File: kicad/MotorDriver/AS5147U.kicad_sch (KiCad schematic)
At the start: 1 part, among them U7 AS5147U

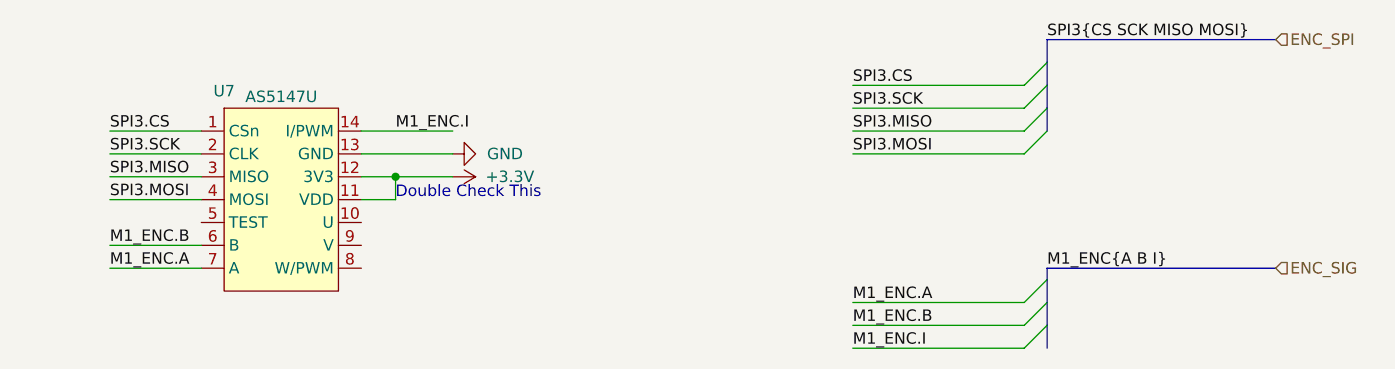
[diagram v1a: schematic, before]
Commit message: Updated the planetary gearbox design. It is much better with retaining rings and bearing support. 95% done with the PCB routing. Need to just do a final routing check and i think I can put the order in
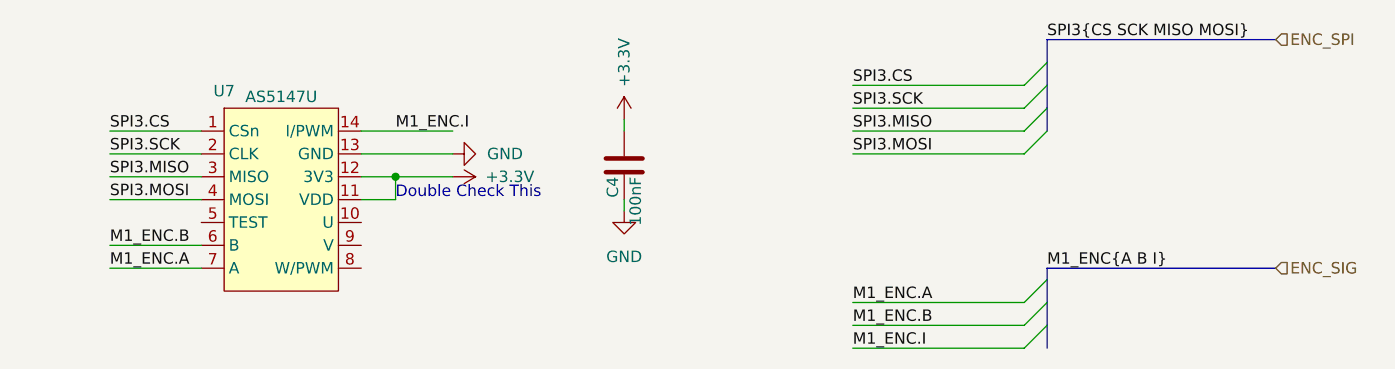
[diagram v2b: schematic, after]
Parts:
- added C4: 100nF, Capacitor_SMD:C_0603_1608Metric, symbol Device:C
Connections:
- net +3.3V: now also C4.2
- net GND: now also C4.1
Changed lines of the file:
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@@
+    (stroke (width 0) (type default))
+  )
+  (wire (pts (xy 177.8 72.39) (xy 177.8 73.66))
     (stroke (width 0) (type default))
   )
@@
   )
   (wire (pts (xy 203.2 71.12) (xy 222.25 71.12))
+    (stroke (width 0) (type default))
+  )
+  (wire (pts (xy 177.8 82.55) (xy 177.8 81.28))
     (stroke (width 0) (type default))
   )
@@
     (effects (font (size 1.27 1.27)) (justify left bottom))
   )
-  (label "M1_ENC.A" (at 203.2 92.71 0)
+  (label "M1_ENC.A" (at 203.2 92.71 0) (fields_autoplaced)
     (effects (font (size 1.27 1.27)) (justify left bottom))
   )
@@
     (effects (font (size 1.27 1.27)) (justify left bottom))
   )
-  (label "SPI3.SCK" (at 203.2 71.12 0)
+  (label "SPI3.SCK" (at 203.2 71.12 0) (fields_autoplaced)
     (effects (font (size 1.27 1.27)) (justify left bottom))
   )
@@
     (effects (font (size 1.27 1.27)) (justify left bottom))
   )
-  (label "SPI3.MISO" (at 203.2 73.66 0)
+  (label "SPI3.MISO" (at 203.2 73.66 0) (fields_autoplaced)
     (effects (font (size 1.27 1.27)) (justify left bottom))
   )
@@
     (effects (font (size 1.27 1.27)) (justify left bottom))
   )
-  (label "SPI3.CS" (at 203.2 68.58 0)
+  (label "SPI3.CS" (at 203.2 68.58 0) (fields_autoplaced)
     (effects (font (size 1.27 1.27)) (justify left bottom))
   )
@@
     (effects (font (size 1.27 1.27)) (justify left))
   )
+  (symbol (lib_id "Device:C") (at 177.8 77.47 180) (unit 1)
+    (in_bom yes) (on_board yes) (dnp no)
+    (property "Reference" "C4" (at 176.53 78.74 90)
+      (effects (font (size 1.27 1.27)) (justify left))
+    )
+    (property "Value" "100nF" (at 179.07 78.74 90)
+      (effects (font (size 1.27 1.27)) (justify left))
+    )
+    (property "Footprint" "Capacitor_SMD:C_0603_1608Metric" (at 176.8348 73.66 0)
+      (effects (font (size 1.27 1.27)) hide)
+    )
+    (property "Datasheet" "~" (at 177.8 77.47 0)
+      (effects (font (size 1.27 1.27)) hide)
+    )
+    (pin "2")
+    (pin "1")
+    (instances
+      (project "MotorDriver"
+        (path "/1fa4c72f-b85f-4d78-9713-26aa572ca2e5"
+          (reference "C4") (unit 1)
+        )
+        (path "/1fa4c72f-b85f-4d78-9713-26aa572ca2e5/c363089b-1b0b-4509-af19-a6f84e71682e"
+          (reference "C28") (unit 1)
+        )
+        (path "/1fa4c72f-b85f-4d78-9713-26aa572ca2e5/a6e3eacb-7b2e-4ad7-94d2-e19606b91cfd"
+          (reference "C3") (unit 1)
+        )
+        (path "/1fa4c72f-b85f-4d78-9713-26aa572ca2e5/bb03fcb5-c814-4162-9fb3-5a1cbb252e46"
+          (reference "C10") (unit 1)
+        )
+      )
+    )
+  )
+  (symbol (lib_id "power:GND") (at 177.8 82.55 0) (unit 1)
+    (in_bom yes) (on_board yes) (dnp no) (fields_autoplaced)
+    (property "Reference" "#PWR037" (at 177.8 88.9 0)
+      (effects (font (size 1.27 1.27)) hide)
+    )
+    (property "Value" "GND" (at 177.8 87.63 0)
+      (effects (font (size 1.27 1.27)))
+    )
+    (property "Footprint" "" (at 177.8 82.55 0)
+      (effects (font (size 1.27 1.27)) hide)
+    )
+    (property "Datasheet" "" (at 177.8 82.55 0)
+      (effects (font (size 1.27 1.27)) hide)
+    )
+    (pin "1")
+    (instances
+      (project "MotorDriver"
+        (path "/1fa4c72f-b85f-4d78-9713-26aa572ca2e5"
+          (reference "#PWR037") (unit 1)
+        )
+        (path "/1fa4c72f-b85f-4d78-9713-26aa572ca2e5/bb03fcb5-c814-4162-9fb3-5a1cbb252e46"
+          (reference "#PWR015") (unit 1)
+        )
+      )
+    )
+  )
+  (symbol (lib_id "power:+3.3V") (at 177.8 72.39 0) (unit 1)
+    (in_bom yes) (on_board yes) (dnp no)
+    (property "Reference" "#PWR036" (at 177.8 76.2 0)
+      (effects (font (size 1.27 1.27)) hide)
+    )
+    (property "Value" "+3.3V" (at 177.8 66.04 90)
+      (effects (font (size 1.27 1.27)))
+    )
+    (property "Footprint" "" (at 177.8 72.39 0)
+      (effects (font (size 1.27 1.27)) hide)
+    )
+    (property "Datasheet" "" (at 177.8 72.39 0)
+      (effects (font (size 1.27 1.27)) hide)
+    )
+    (pin "1")
+    (instances
+      (project "MotorDriver"
+        (path "/1fa4c72f-b85f-4d78-9713-26aa572ca2e5"
+          (reference "#PWR036") (unit 1)
+        )
+        (path "/1fa4c72f-b85f-4d78-9713-26aa572ca2e5/bb03fcb5-c814-4162-9fb3-5a1cbb252e46"
+          (reference "#PWR012") (unit 1)
+        )
+      )
+    )
+  )
   (symbol (lib_id "TylerLib:AS5147U-HTSM") (at 139.7 69.85 0) (unit 1)

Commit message: PCB ordered
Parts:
- C4: value 100nF -> 0.1uF
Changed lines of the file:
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@@
   (symbol (lib_id "Device:C") (at 177.8 77.47 180) (unit 1)
     (in_bom yes) (on_board yes) (dnp no)
-    (property "Reference" "C4" (at 176.53 78.74 90)
+    (property "Reference" "C4" (at 182.245 74.93 0)
       (effects (font (size 1.27 1.27)) (justify left))
     )
-    (property "Value" "100nF" (at 179.07 78.74 90)
+    (property "Value" "0.1uF" (at 184.785 80.01 0)
       (effects (font (size 1.27 1.27)) (justify left))
     )
@@
       (effects (font (size 1.27 1.27)) hide)
     )
-    (property "Datasheet" "~" (at 177.8 77.47 0)
+    (property "Datasheet" "https://www.digikey.com/en/products/detail/samsung-electro-mechanics/CL10B104KB8NNWC/3887593" (at 177.8 77.47 0)
       (effects (font (size 1.27 1.27)) hide)
     )
@@
       (effects (font (size 1.27 1.27)) hide)
     )
-    (property "Datasheet" "" (at 139.7 69.85 0)
+    (property "Datasheet" "https://www.digikey.com/en/products/detail/ams-osram-usa-inc/AS5147U-HTSM/10324300" (at 139.7 69.85 0)
       (effects (font (size 1.27 1.27)) hide)
     )

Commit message: Working on some of the solidworks model, new urdf, working on the motor drive board a little
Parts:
- added TP2 (x7): TestPoint, TestPoint:TestPoint_Pad_D1.0mm, symbol Connector:TestPoint
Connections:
- net M1_ENC.A: now also TP2.1
- net M1_ENC.B: now also TP2.1
- net M1_ENC.I: now also TP2.1
- net SPI3.CS: now also TP2.1
- net SPI3.MISO: now also TP2.1
- net SPI3.MOSI: now also TP2.1
- net SPI3.SCK: now also TP2.1
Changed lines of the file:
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@@
     (stroke (width 0) (type default))
   )
-  (wire (pts (xy 130.81 78.74) (xy 120.65 78.74))
+  (wire (pts (xy 130.81 78.74) (xy 116.84 78.74))
     (stroke (width 0) (type default))
   )
@@
     (stroke (width 0) (type default))
   )
-  (wire (pts (xy 130.81 76.2) (xy 120.65 76.2))
+  (wire (pts (xy 130.81 76.2) (xy 118.745 76.2))
     (stroke (width 0) (type default))
   )
@@
     (stroke (width 0) (type default))
   )
-  (wire (pts (xy 130.81 88.9) (xy 120.65 88.9))
+  (wire (pts (xy 130.81 88.9) (xy 118.745 88.9))
     (stroke (width 0) (type default))
   )
@@
   (hierarchical_label "ENC_SIG" (shape input) (at 250.19 88.9 0) (fields_autoplaced)
     (effects (font (size 1.27 1.27)) (justify left))
+  )
+  (symbol (lib_id "Connector:TestPoint") (at 120.65 73.66 90) (unit 1)
+    (in_bom yes) (on_board yes) (dnp no)
+    (property "Reference" "TP2" (at 115.57 74.93 0)
+      (effects (font (size 1.27 1.27)) (justify left))
+    )
+    (property "Value" "TestPoint" (at 118.618 71.12 0)
+      (effects (font (size 1.27 1.27)) (justify left) hide)
+    )
+    (property "Footprint" "TestPoint:TestPoint_Pad_D1.0mm" (at 120.65 68.58 0)
+      (effects (font (size 1.27 1.27)) hide)
+    )
+    (property "Datasheet" "~" (at 120.65 68.58 0)
+      (effects (font (size 1.27 1.27)) hide)
+    )
+    (pin "1")
+    (instances
+      (project "MotorDriver"
+        (path "/1fa4c72f-b85f-4d78-9713-26aa572ca2e5"
+          (reference "TP2") (unit 1)
+        )
+        (path "/1fa4c72f-b85f-4d78-9713-26aa572ca2e5/c363089b-1b0b-4509-af19-a6f84e71682e"
+          (reference "TP5") (unit 1)
+        )
+        (path "/1fa4c72f-b85f-4d78-9713-26aa572ca2e5/bb03fcb5-c814-4162-9fb3-5a1cbb252e46"
+          (reference "TP1") (unit 1)
+        )
+      )
+    )
   )
   (symbol (lib_id "Device:C") (at 177.8 77.47 180) (unit 1)
@@
         (path "/1fa4c72f-b85f-4d78-9713-26aa572ca2e5/bb03fcb5-c814-4162-9fb3-5a1cbb252e46"
           (reference "#PWR012") (unit 1)
+        )
+      )
+    )
+  )
+  (symbol (lib_id "Connector:TestPoint") (at 116.84 78.74 90) (unit 1)
+    (in_bom yes) (on_board yes) (dnp no)
+    (property "Reference" "TP2" (at 111.76 80.01 0)
+      (effects (font (size 1.27 1.27)) (justify left))
+    )
+    (property "Value" "TestPoint" (at 114.808 76.2 0)
+      (effects (font (size 1.27 1.27)) (justify left) hide)
+    )
+    (property "Footprint" "TestPoint:TestPoint_Pad_D1.0mm" (at 116.84 73.66 0)
+      (effects (font (size 1.27 1.27)) hide)
+    )
+    (property "Datasheet" "~" (at 116.84 73.66 0)
+      (effects (font (size 1.27 1.27)) hide)
+    )
+    (pin "1")
+    (instances
+      (project "MotorDriver"
+        (path "/1fa4c72f-b85f-4d78-9713-26aa572ca2e5"
+          (reference "TP2") (unit 1)
+        )
+        (path "/1fa4c72f-b85f-4d78-9713-26aa572ca2e5/c363089b-1b0b-4509-af19-a6f84e71682e"
+          (reference "TP5") (unit 1)
+        )
+        (path "/1fa4c72f-b85f-4d78-9713-26aa572ca2e5/bb03fcb5-c814-4162-9fb3-5a1cbb252e46"
+          (reference "TP3") (unit 1)
         )
       )
@@
     )
   )
+  (symbol (lib_id "Connector:TestPoint") (at 120.65 86.36 90) (unit 1)
+    (in_bom yes) (on_board yes) (dnp no)
+    (property "Reference" "TP2" (at 115.57 87.63 0)
+      (effects (font (size 1.27 1.27)) (justify left))
+    )
+    (property "Value" "TestPoint" (at 118.618 83.82 0)
+      (effects (font (size 1.27 1.27)) (justify left) hide)
+    )
+    (property "Footprint" "TestPoint:TestPoint_Pad_D1.0mm" (at 120.65 81.28 0)
+      (effects (font (size 1.27 1.27)) hide)
+    )
+    (property "Datasheet" "~" (at 120.65 81.28 0)
+      (effects (font (size 1.27 1.27)) hide)
+    )
+    (pin "1")
+    (instances
+      (project "MotorDriver"
+        (path "/1fa4c72f-b85f-4d78-9713-26aa572ca2e5"
+          (reference "TP2") (unit 1)
+        )
+        (path "/1fa4c72f-b85f-4d78-9713-26aa572ca2e5/c363089b-1b0b-4509-af19-a6f84e71682e"
+          (reference "TP5") (unit 1)
+        )
+        (path "/1fa4c72f-b85f-4d78-9713-26aa572ca2e5/bb03fcb5-c814-4162-9fb3-5a1cbb252e46"
+          (reference "TP7") (unit 1)
+        )
+      )
+    )
+  )
+  (symbol (lib_id "Connector:TestPoint") (at 118.745 88.9 90) (unit 1)
+    (in_bom yes) (on_board yes) (dnp no)
+    (property "Reference" "TP2" (at 113.665 90.17 0)
+      (effects (font (size 1.27 1.27)) (justify left))
+    )
+    (property "Value" "TestPoint" (at 116.713 86.36 0)
+      (effects (font (size 1.27 1.27)) (justify left) hide)
+    )
+    (property "Footprint" "TestPoint:TestPoint_Pad_D1.0mm" (at 118.745 83.82 0)
+      (effects (font (size 1.27 1.27)) hide)
+    )
+    (property "Datasheet" "~" (at 118.745 83.82 0)
+      (effects (font (size 1.27 1.27)) hide)
+    )
+    (pin "1")
+    (instances
+      (project "MotorDriver"
+        (path "/1fa4c72f-b85f-4d78-9713-26aa572ca2e5"
+          (reference "TP2") (unit 1)
+        )
+        (path "/1fa4c72f-b85f-4d78-9713-26aa572ca2e5/c363089b-1b0b-4509-af19-a6f84e71682e"
+          (reference "TP5") (unit 1)
+        )
+        (path "/1fa4c72f-b85f-4d78-9713-26aa572ca2e5/bb03fcb5-c814-4162-9fb3-5a1cbb252e46"
+          (reference "TP10") (unit 1)
+        )
+      )
+    )
+  )
   (symbol (lib_id "power:GND") (at 158.75 76.2 90) (unit 1)
     (in_bom yes) (on_board yes) (dnp no) (fields_autoplaced)
@@
         )
       )
+    )
+  )
+  (symbol (lib_id "Connector:TestPoint") (at 120.65 81.28 90) (unit 1)
+    (in_bom yes) (on_board yes) (dnp no)
+    (property "Reference" "TP2" (at 115.57 82.55 0)
+      (effects (font (size 1.27 1.27)) (justify left))
+    )
+    (property "Value" "TestPoint" (at 118.618 78.74 0)
+      (effects (font (size 1.27 1.27)) (justify left) hide)
+    )
+    (property "Footprint" "TestPoint:TestPoint_Pad_D1.0mm" (at 120.65 76.2 0)
+      (effects (font (size 1.27 1.27)) hide)
+    )
+    (property "Datasheet" "~" (at 120.65 76.2 0)
+      (effects (font (size 1.27 1.27)) hide)
+    )
+    (pin "1")
+    (instances
+      (project "MotorDriver"
+        (path "/1fa4c72f-b85f-4d78-9713-26aa572ca2e5"
+          (reference "TP2") (unit 1)
+        )
+        (path "/1fa4c72f-b85f-4d78-9713-26aa572ca2e5/c363089b-1b0b-4509-af19-a6f84e71682e"
+          (reference "TP5") (unit 1)
+        )
+        (path "/1fa4c72f-b85f-4d78-9713-26aa572ca2e5/bb03fcb5-c814-4162-9fb3-5a1cbb252e46"
+          (reference "TP4") (unit 1)
+        )
+      )
+    )
+  )
+  (symbol (lib_id "Connector:TestPoint") (at 158.75 73.66 270) (unit 1)
+    (in_bom yes) (on_board yes) (dnp no)
+    (property "Reference" "TP2" (at 163.83 72.39 0)
+      (effects (font (size 1.27 1.27)) (justify left))
+    )
+    (property "Value" "TestPoint" (at 160.782 76.2 0)
+      (effects (font (size 1.27 1.27)) (justify left) hide)
+    )
+    (property "Footprint" "TestPoint:TestPoint_Pad_D1.0mm" (at 158.75 78.74 0)
+      (effects (font (size 1.27 1.27)) hide)
+    )
+    (property "Datasheet" "~" (at 158.75 78.74 0)
+      (effects (font (size 1.27 1.27)) hide)
+    )
+    (pin "1")
+    (instances
+      (project "MotorDriver"
+        (path "/1fa4c72f-b85f-4d78-9713-26aa572ca2e5"
+          (reference "TP2") (unit 1)
+        )
+        (path "/1fa4c72f-b85f-4d78-9713-26aa572ca2e5/c363089b-1b0b-4509-af19-a6f84e71682e"
+          (reference "TP5") (unit 1)
+        )
+        (path "/1fa4c72f-b85f-4d78-9713-26aa572ca2e5/bb03fcb5-c814-4162-9fb3-5a1cbb252e46"
+          (reference "TP13") (unit 1)
+        )
+      )
+    )
+  )
+  (symbol (lib_id "Connector:TestPoint") (at 118.745 76.2 90) (unit 1)
+    (in_bom yes) (on_board yes) (dnp no)
+    (property "Reference" "TP2" (at 113.665 77.47 0)
+      (effects (font (size 1.27 1.27)) (justify left))
+    )
+    (property "Value" "TestPoint" (at 116.713 73.66 0)
+      (effects (font (size 1.27 1.27)) (justify left) hide)
+    )
+    (property "Footprint" "TestPoint:TestPoint_Pad_D1.0mm" (at 118.745 71.12 0)
+      (effects (font (size 1.27 1.27)) hide)
+    )
+    (property "Datasheet" "~" (at 118.745 71.12 0)
+      (effects (font (size 1.27 1.27)) hide)
+    )
+    (pin "1")
+    (instances
+      (project "MotorDriver"
+        (path "/1fa4c72f-b85f-4d78-9713-26aa572ca2e5"
+          (reference "TP2") (unit 1)
+        )
+        (path "/1fa4c72f-b85f-4d78-9713-26aa572ca2e5/c363089b-1b0b-4509-af19-a6f84e71682e"
+          (reference "TP5") (unit 1)
+        )
+        (path "/1fa4c72f-b85f-4d78-9713-26aa572ca2e5/bb03fcb5-c814-4162-9fb3-5a1cbb252e46"
+          (reference "TP2") (unit 1)
+        )
+      )
